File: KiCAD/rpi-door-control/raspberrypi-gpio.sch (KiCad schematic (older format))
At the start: 21 parts, among them P1 CONN_13X2

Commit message: redrew schematic to make it follow more standard conventions
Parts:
- removed P? (x3): CONN_2X2, symbol CONN_2X2
- removed P?: CONN_6X2, symbol CONN_6X2
- removed U?: RELAY, symbol RELAY
- added J1: RJ45, symbol RJ45
- added P2, P3, P4: CONN_2, symbol CONN_2
- added U1: RELAY, ~, symbol RELAY
- gave numbers to parts that had none: 15
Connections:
- net labels added: +12V GND, RFID TXD
- net labels removed: RFID DATA
- wire segments 78 -> 77
- no-connect marks 7 -> 21
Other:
- note added: "12V Power\nSupply"
- note added: "Push-to-lock \nButton"
- note removed: "+"
- note removed: "-"
- note removed: "12V Power Supply"
- note removed: "Lock Timer Button"
- moved on the sheet: D1, D2, D3, D4, D5, P1, Q1, R1, R2, R3, R4, R5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

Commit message: Make multi-sheet and fix stuff
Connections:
- net labels removed: +12V GND
- wire segments 77 -> 80
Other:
- moved on the sheet: D1, D2, D3, D4, D5, J1, P1, P2, P3, P4, Q1, R1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

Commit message: Added datasheets, start footprint designs
Merged in changes from svn repo
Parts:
- D5: dipmicro# (none) -> DE3275
- P3, P4: dipmicro# (none) -> DE1632
- Q1: dipmicro# (none) -> DE3069
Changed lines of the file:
@@
 Sheet 1 2
 Title "Door Controller"
-Date "19 mar 2014"
+Date "22 mar 2014"
 Rev "0.4"
 Comp "Shawn Wilson"
@@
 F 1 "1N4007" H 8150 3600 40  0000 L CNN
 F 2 "DO7" H 8300 3850 30  0001 C CNN
-F 3 "" H 8300 3700 60  0001 C CNN
+F 3 "1N4007.pdf" H 8300 3700 60  0001 C CNN
+F 4 "DE3275" H 8300 3700 60  0001 C CNN "dipmicro#"
 	1    8300 3700
 	1    0    0    -1
@@
 F 1 "N3904" H 7250 3800 50  0000 R CNN
 F 2 "~" H 7250 3650 60  0000 C CNN
-F 3 "~" H 7250 3650 60  0000 C CNN
+F 3 "2N3904.pdf" H 7100 3350 60  0001 C CNN
+F 4 "DE3069" H 7250 3650 60  0001 C CNN "dipmicro#"
 	1    7250 3650
 	1    0    0    -1
@@
 F 1 "CONN_2" V 1150 1350 40  0000 C CNN
 F 2 "" H 1100 1350 60  0000 C CNN
-F 3 "" H 1100 1350 60  0000 C CNN
+F 3 "Switchcraft-35RAPC2AVN4-datasheet.pdf" H 800 850 60  0001 C CNN
 	1    1100 1350
 	-1   0    0    1
@@
 F 2 "" H 9800 2250 60  0000 C CNN
 F 3 "" H 9800 2250 60  0000 C CNN
+F 4 "DE1632" V 9800 2250 60  0001 C CNN "dipmicro#"
 	1    9800 2250
 	1    0    0    -1
@@
 F 2 "" H 5300 1550 60  0000 C CNN
 F 3 "" H 5300 1550 60  0000 C CNN
+F 4 "DE1632" V 5300 1550 60  0001 C CNN "dipmicro#"
 	1    5300 1550
 	-1   0    0    1

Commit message: Start of v0.5 of schematic.  Converted the circuit to isolate 12V with an opto-isolator.  Will redraw the PCB to be just a bullshit square linked by a ribbon cable or something so it can be milled with a 1.6mm cutter
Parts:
- removed Q1: N3904, ~, symbol NPN
- added IC?: PC817, DIP4, symbol PC817
- added Q?: PN2222A, TO92, symbol PN2222A
- added Q?: 2N3904, symbol 2N3904
- added R?: 180, ~, symbol R
- added R?: 3.3k???, ~, symbol R
- added R?: 150???, ~, symbol R
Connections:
- net labels added: GNDPWR
- wire segments 80 -> 94
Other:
- moved on the sheet: D4, D5, P3, R7, R8, U1

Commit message: First try at drawing schematic v0.5
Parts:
- removed Q?: 2N3904, symbol 2N3904
- removed R7: 1K, symbol R
- removed R?: 180, ~, symbol R
- added Q1: 2N3904, ~, symbol NPN
- R6: value 330 -> ?????
- gave numbers to parts that had none: 4
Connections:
- wire segments 94 -> 96
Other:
- note added: "POWER"
- note removed: "Maglock\nPower"
- moved on the sheet: D1, D2, D3, D4, D5, IC1, P3, P4, Q2, R11, R4, R5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

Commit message: Created version 0.6
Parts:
- removed IC1: PC817, DIP4, symbol PC817
- removed Q2: PN2222A, TO92, symbol PN2222A
- added D8: 1N4007, DO7, symbol 1N4004
- added IC1: 4N35, DIP6, symbol 4N35
- added Q2: 2N3904, ~, symbol NPN
- added R12: 680, ~, symbol R
- R11: value 3.3k??? -> 330
- R6: value ????? -> 2K
- R7: value 150??? -> 10K
- R8: value 2K -> 200
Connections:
- wire segments 96 -> 85
- no-connect marks 21 -> 22
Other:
- moved on the sheet: D3, D4, D5, P3, P4, Q1, R11, R6, R7, R8, U1

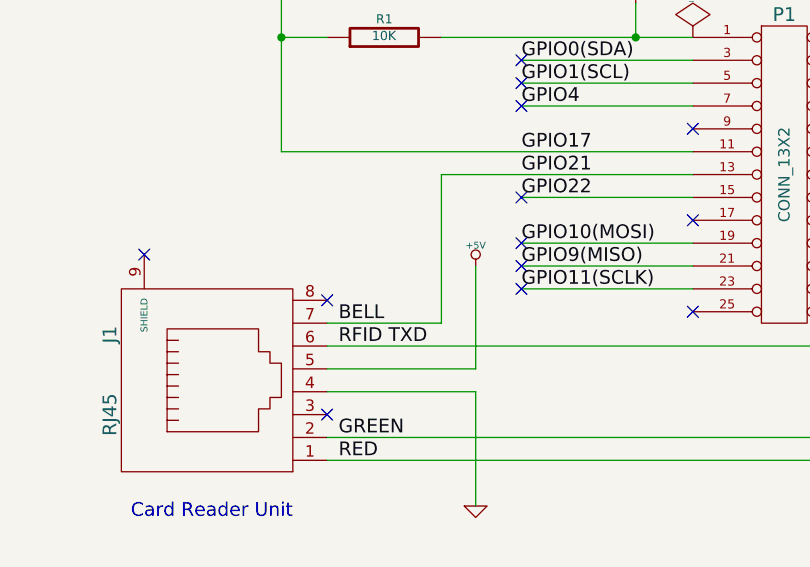
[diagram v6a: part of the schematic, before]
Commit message: drew up single sided board but can't connect grounds.  Needs serious rerouting
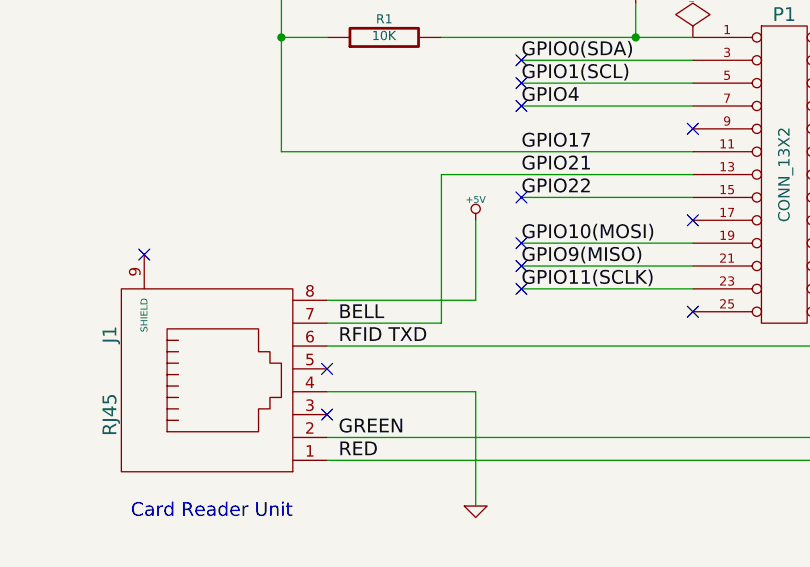
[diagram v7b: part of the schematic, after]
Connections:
- net +5V: now also J1.8; no longer J1.5
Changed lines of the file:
@@
 Sheet 1 2
 Title "Door Controller"
-Date "10 may 2014"
+Date "17 may 2014"
 Rev "0.6"
 Comp "Shawn Wilson"
@@
 	0    -1   -1   0
 $EndComp
-NoConn ~ 1800 3800
 NoConn ~ 1000 3600
 NoConn ~ 2650 3650
@@
 L +5V #PWR013
 U 1 1 532A2790
-P 2450 3650
-F 0 "#PWR013" H 2450 3740 20  0001 C CNN
-F 1 "+5V" H 2450 3740 30  0000 C CNN
-F 2 "" H 2450 3650 60  0000 C CNN
-F 3 "" H 2450 3650 60  0000 C CNN
-	1    2450 3650
+P 2450 3450
+F 0 "#PWR013" H 2450 3540 20  0001 C CNN
+F 1 "+5V" H 2450 3540 30  0000 C CNN
+F 2 "" H 2450 3450 60  0000 C CNN
+F 3 "" H 2450 3450 60  0000 C CNN
+	1    2450 3450
 	1    0    0    -1
 $EndComp
@@
 	5000 1500 5000 1800
 Wire Wire Line
-	2450 4100 1800 4100
-Wire Wire Line
 	4200 2850 5250 2850
 Wire Wire Line
@@
 Wire Wire Line
 	4200 2650 6800 2650
-Wire Wire Line
-	2450 3650 2450 4100
 Wire Wire Line
 	2450 4200 2450 4700
@@
 Wire Wire Line
 	8000 2200 7600 2200
+Wire Wire Line
+	1800 3800 2450 3800
+Wire Wire Line
+	2450 3800 2450 3450
+NoConn ~ 1800 4100
 $EndSCHEMATC
